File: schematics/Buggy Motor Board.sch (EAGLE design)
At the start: 48 parts, among them CON0 M025MM, CON1 M025MM, U2 MCP2562, U3 MCP2562, X1 MICROSD, X2 5566-24, X3 5566-24, Y1 16MHz

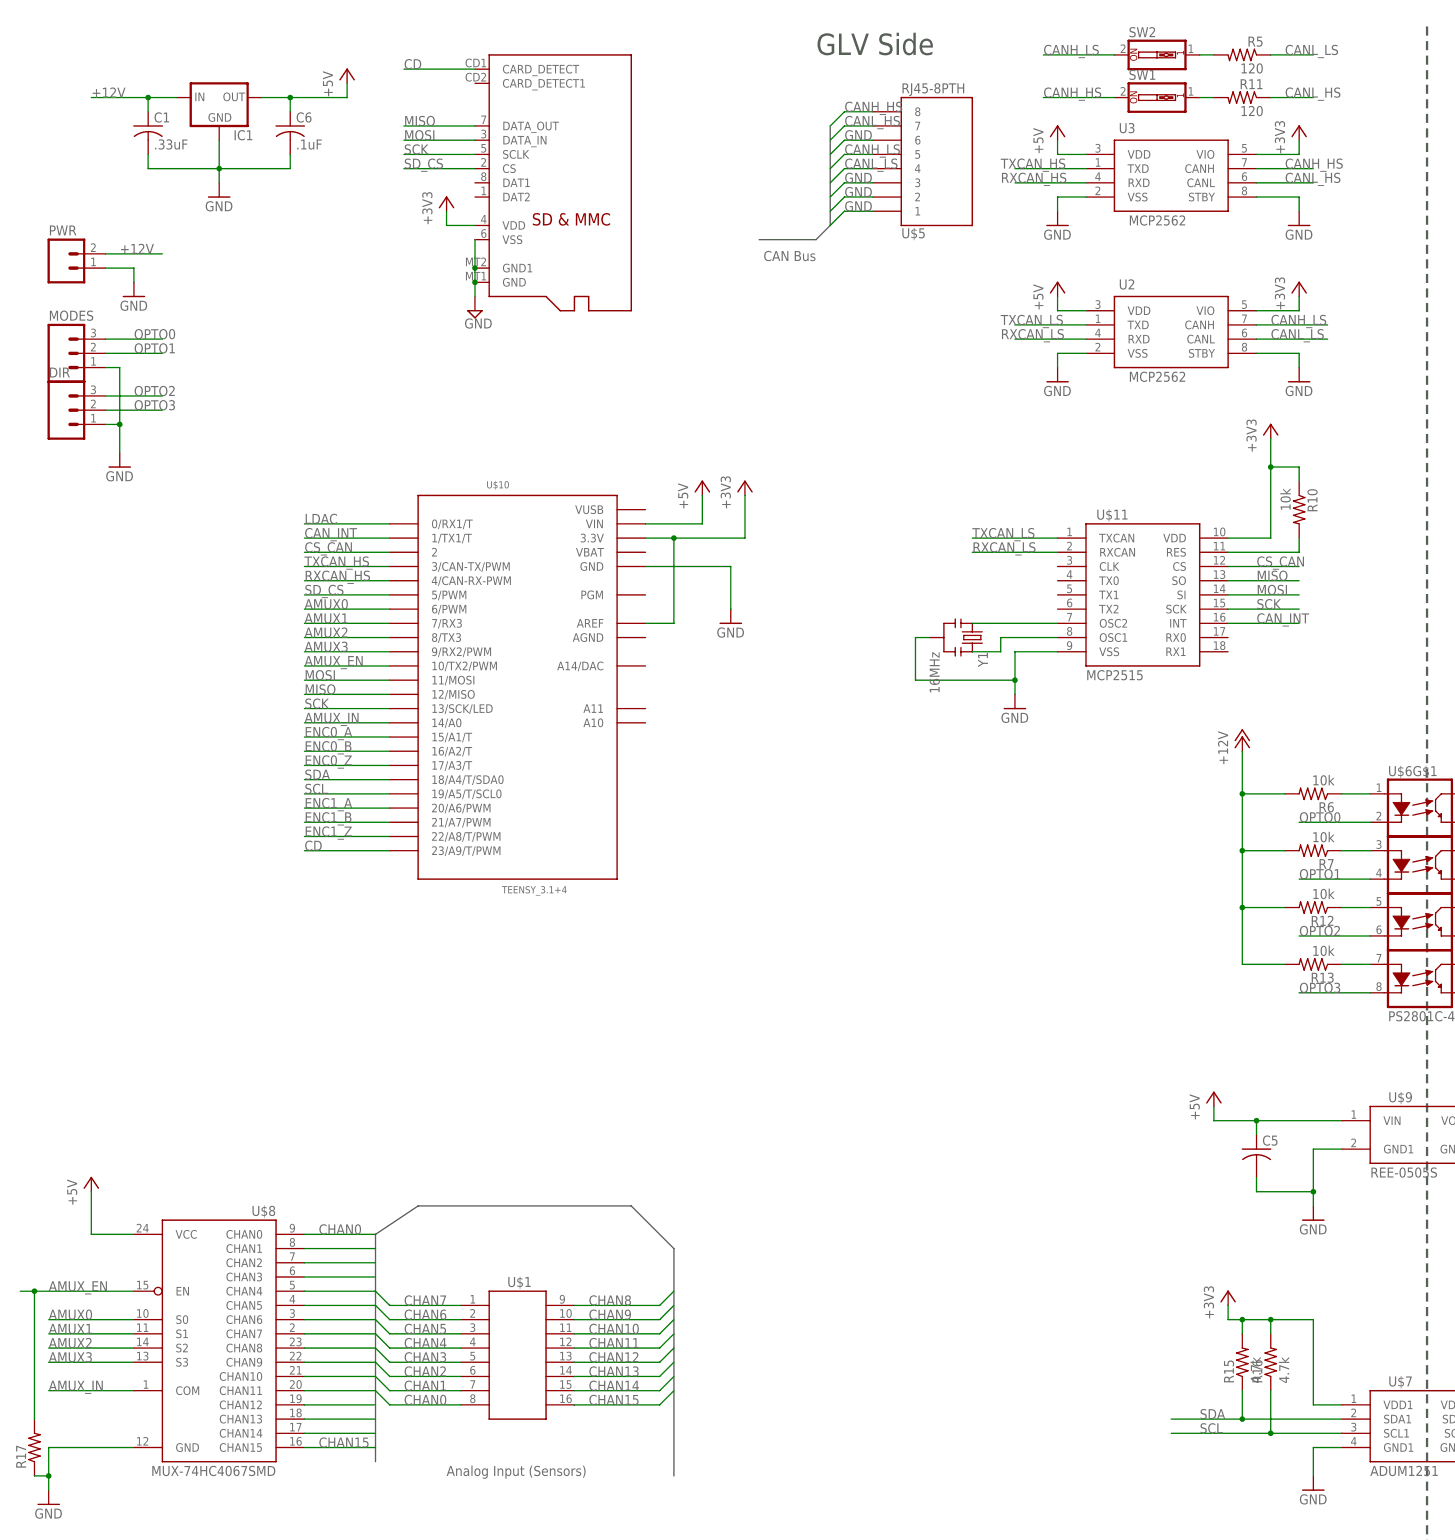
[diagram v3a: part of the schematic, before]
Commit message: Tested to be working with motors
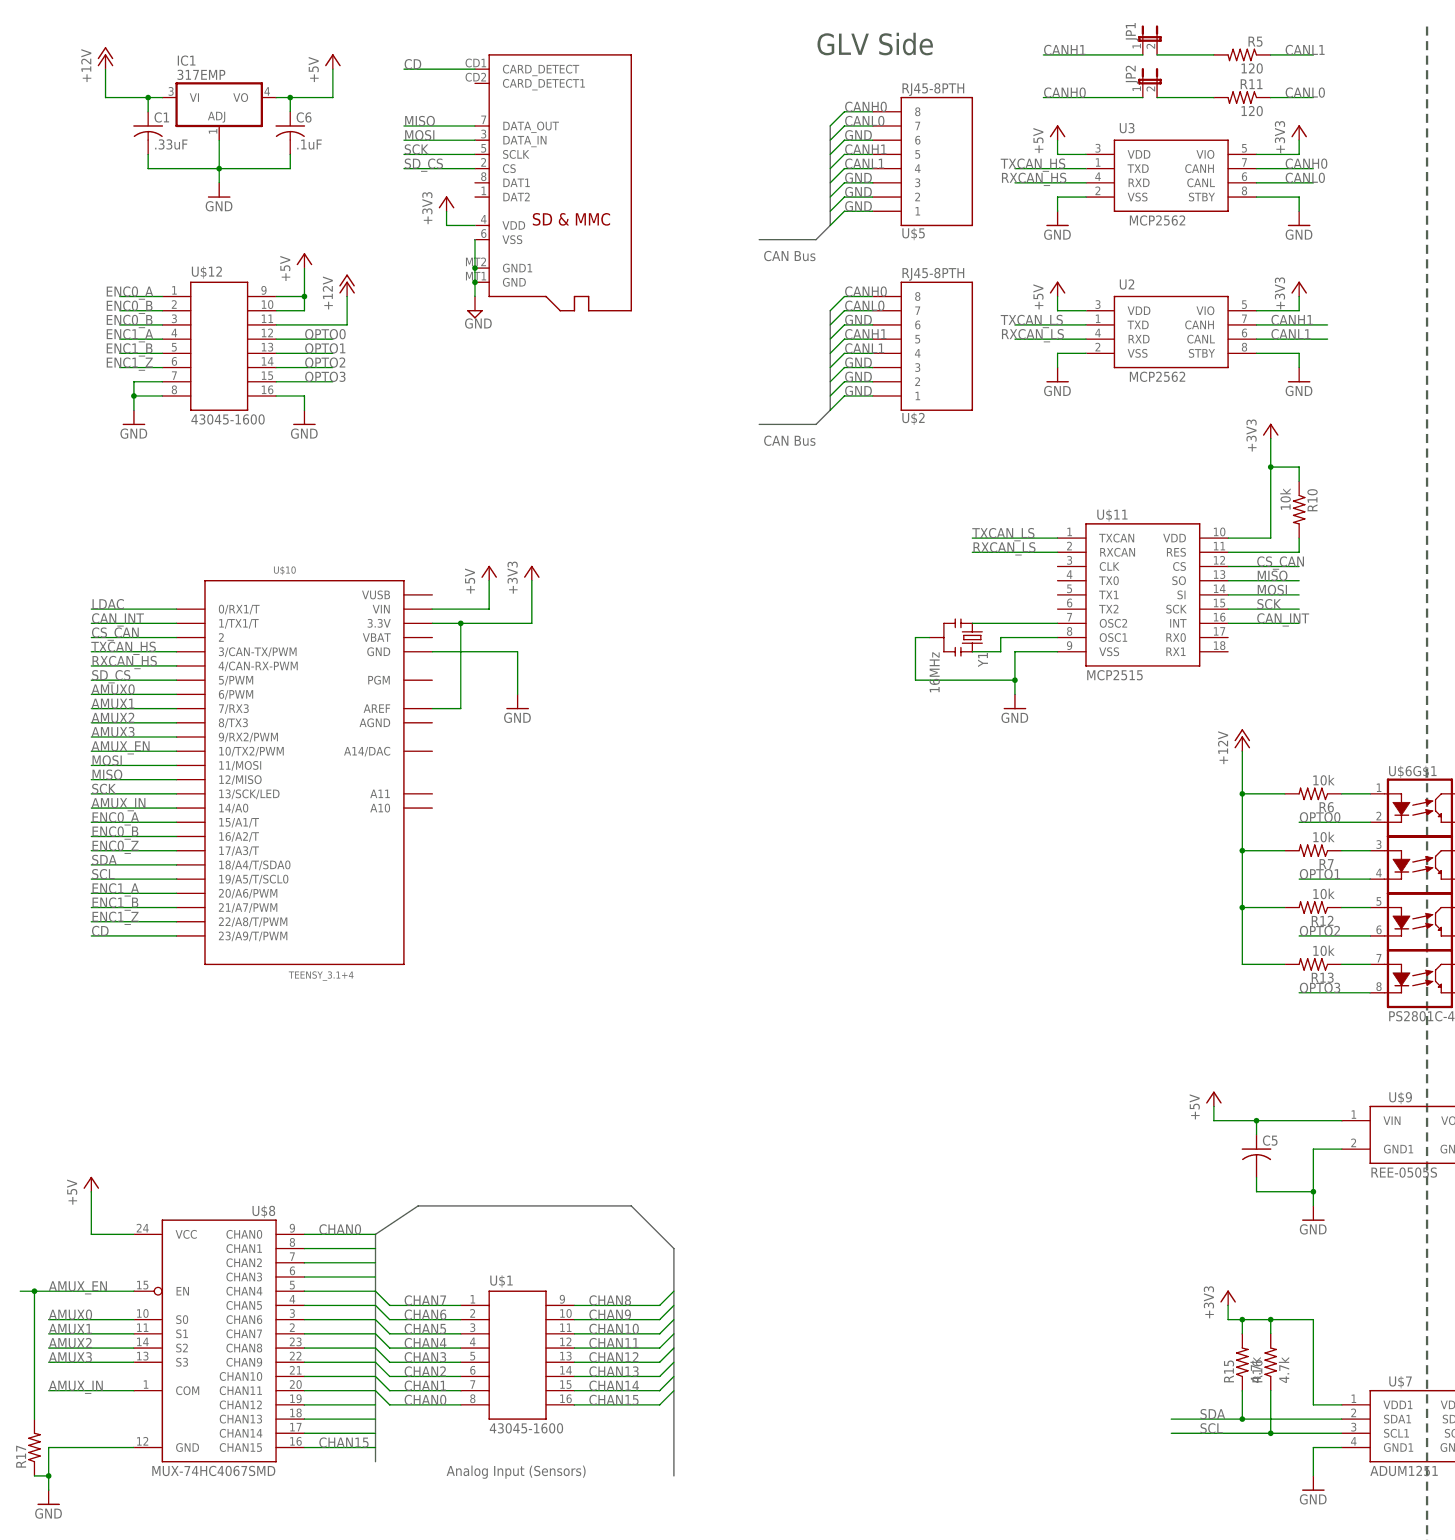
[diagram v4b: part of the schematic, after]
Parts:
- removed DIR, MODES: (no value), SparkFun-Connectors:M03SCREW_LOCK
- removed PWR: M023.5MM_LOCK, SparkFun-Connectors:M023.5MM_LOCK
- removed SW1, SW2: (no value), special:SW_DIP-1
- added JP1, JP2: (no value), jumper:JP1E
- added U$12: 43045-1600, Wetmelon-Connectors:43045-1600
- added U$2: RJ45-8PTH, SparkFun-Connectors:RJ45-8PTH
- IC1: value (none) -> 317EMP; device SparkFun-PowerIC:V_REG_78XXSIDE -> linear:317EMP
- U$1: value WM9300 -> 43045-1600; device Wetmelon-Connectors:WM9300 -> Wetmelon-Connectors:43045-1600
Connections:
- removed net CANH_HS: SW1.2, U$5.8, U3.CANH
- removed net CANH_LS: SW2.2, U$5.5, U2.CANH
- removed net CANL_HS: R11.1, U$5.7, U3.CANL
- removed net CANL_LS: R5.1, U$5.4, U2.CANL
- new net CANH0: JP2.1, U$2.8, U$5.8, U3.CANH
- new net CANH1: JP1.1, U$2.5, U$5.5, U2.CANH
- new net CANL0: R11.1, U$2.7, U$5.7, U3.CANL
- new net CANL1: R5.1, U$2.4, U$5.4, U2.CANL
- net +12V: now also IC1.VI, U$12.P$11; no longer IC1.IN, PWR.2
- net +5V: now also IC1.VO, U$12.P$10, U$12.P$9; no longer IC1.OUT
- net ENC0_A: now also U$12.P$1
- net ENC0_B: now also U$12.P$2
- net ENC0_Z: now also U$12.P$3
- net ENC1_A: now also U$12.P$4
- net ENC1_B: now also U$12.P$5
- net ENC1_Z: now also U$12.P$6
- net GND: now also IC1.ADJ, U$12.P$16, U$12.P$7, U$12.P$8, U$2.1, U$2.2, U$2.3, U$2.6; no longer DIR.1, IC1.GND, MODES.1, PWR.1
- net N$1: now also JP1.2; no longer SW2.1
- net N$13: now also JP2.2; no longer SW1.1
- net OPTO0: now also U$12.P$12; no longer MODES.3
- net OPTO1: now also U$12.P$13; no longer MODES.2
- net OPTO2: now also U$12.P$14; no longer DIR.3
- net OPTO3: now also U$12.P$15; no longer DIR.2
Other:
- moved on the sheet: U$10
